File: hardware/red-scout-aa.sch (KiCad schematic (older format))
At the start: 2 parts, among them U1 SM200

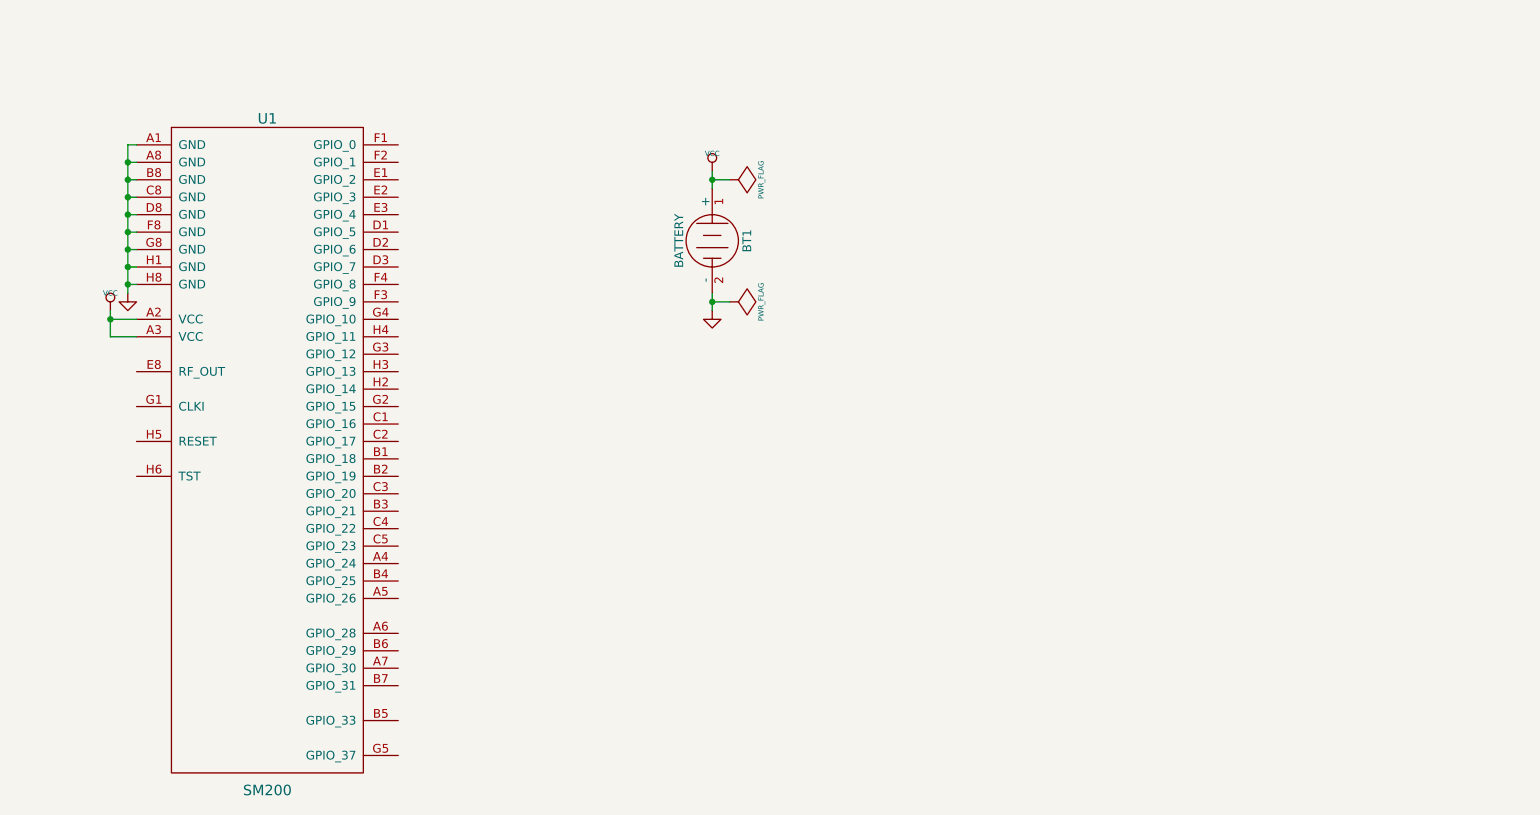
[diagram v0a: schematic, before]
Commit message: Added snap connectors and LEDs.
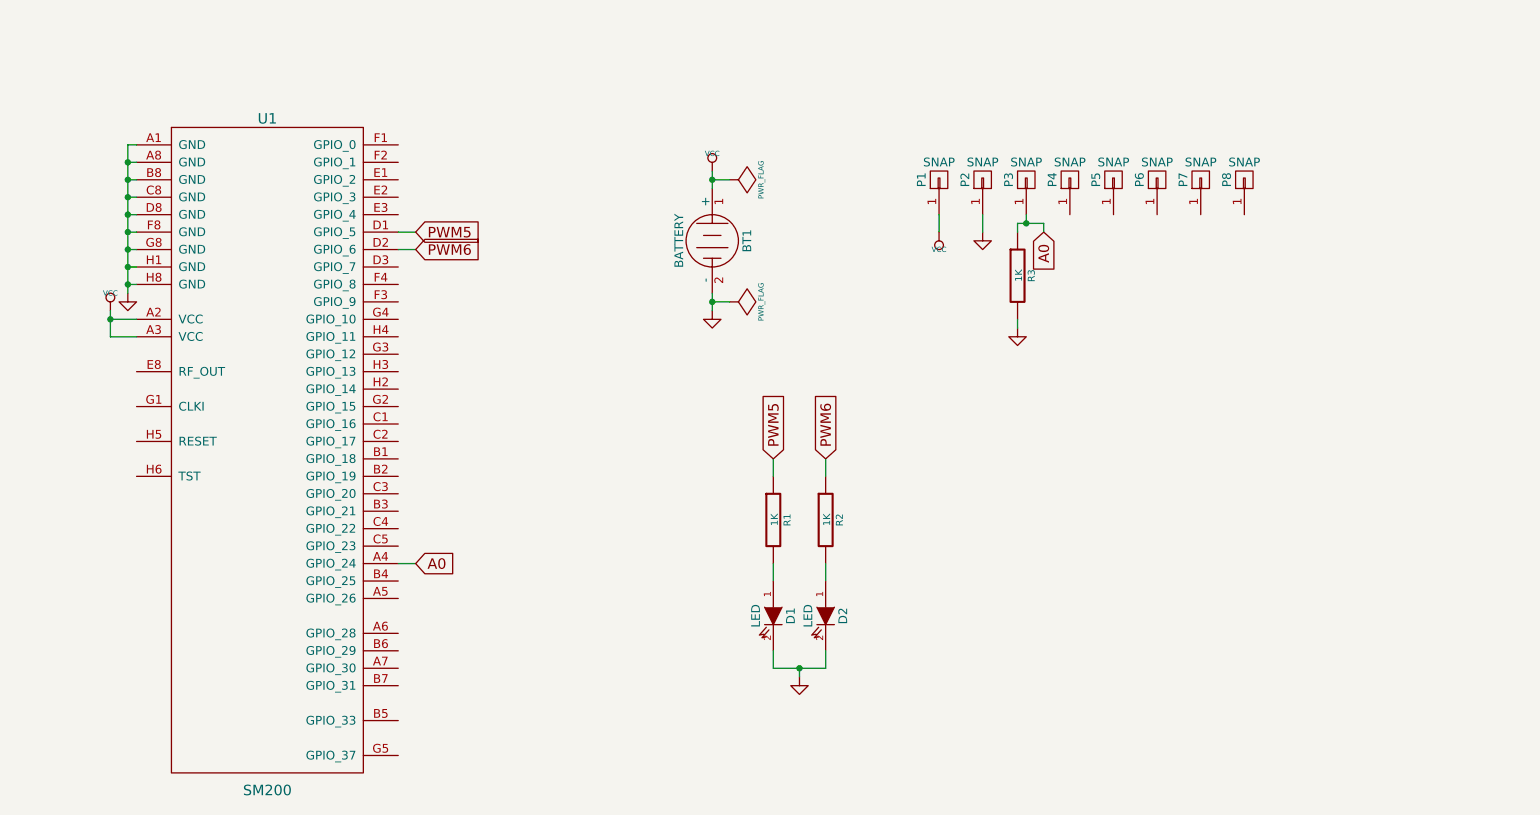
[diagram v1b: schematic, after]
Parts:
- added D1, D2: LED, symbol LED
- added P1, P2, P3, P4, P5, P6, P7, P8: SNAP, symbol CONN_01X01
- added R1, R2, R3: 1K, symbol R
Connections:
- net GND: now also D1.2 (K), D2.2 (K), P2.1 (P1), R3.2
- net VCC: now also P1.1 (P1)
- net A0: now reaches U1.A4 (GPIO_24)
- net A0: now also P3.1 (P1), R3.1
- net PWM5: now reaches U1.D1 (GPIO_5)
- net PWM5: now also R1.1
- net PWM6: now reaches U1.D2 (GPIO_6)
- net PWM6: now also R2.1
- new net: D1.1 (A), R1.2
- new net: D2.1 (A), R2.2
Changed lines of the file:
@@
 	1    0    0    -1
 $EndComp
-Wire Wire Line
-	2800 1550 2750 1550
-Wire Wire Line
-	2750 1550 2750 2400
-Wire Wire Line
-	2750 2350 2800 2350
-Wire Wire Line
-	2800 2250 2750 2250
-Connection ~ 2750 2250
-Wire Wire Line
-	2750 2150 2800 2150
-Connection ~ 2750 2150
-Wire Wire Line
-	2800 2050 2750 2050
-Connection ~ 2750 2050
-Wire Wire Line
-	2750 1950 2800 1950
-Connection ~ 2750 1950
-Wire Wire Line
-	2800 1850 2750 1850
-Connection ~ 2750 1850
-Wire Wire Line
-	2750 1750 2800 1750
-Connection ~ 2750 1750
-Wire Wire Line
-	2800 1650 2750 1650
-Connection ~ 2750 1650
-Connection ~ 2750 2350
 $Comp
 L BATTERY BT1
@@
 	1    0    0    -1
 $EndComp
-Wire Wire Line
-	6100 1800 6100 1700
-Wire Wire Line
-	6100 2400 6100 2500
 $Comp
 L VCC #PWR04
@@
 	1    0    0    -1
 $EndComp
-Wire Wire Line
-	2650 2500 2650 2650
-Wire Wire Line
-	2650 2550 2800 2550
-Wire Wire Line
-	2650 2650 2800 2650
-Connection ~ 2650 2550
 $Comp
 L PWR_FLAG #FLG05
@@
 	0    1    1    0
 $EndComp
+$Comp
+L R R3
+U 1 1 54F7F6ED
+P 7850 2300
+F 0 "R3" V 7930 2300 40  0000 C CNN
+F 1 "1K" V 7857 2301 40  0000 C CNN
+F 2 "" V 7780 2300 30  0000 C CNN
+F 3 "" H 7850 2300 30  0000 C CNN
+	1    7850 2300
+	1    0    0    -1
+$EndComp
+$Comp
+L CONN_01X01 P1
+U 1 1 54F7F75E
+P 7400 1750
+F 0 "P1" H 7400 1850 50  0000 C CNN
+F 1 "SNAP" V 7500 1750 50  0000 C CNN
+F 2 "" H 7400 1750 60  0000 C CNN
+F 3 "" H 7400 1750 60  0000 C CNN
+	1    7400 1750
+	0    -1   -1   0
+$EndComp
+$Comp
+L CONN_01X01 P2
+U 1 1 54F7F9DB
+P 7650 1750
+F 0 "P2" H 7650 1850 50  0000 C CNN
+F 1 "SNAP" V 7750 1750 50  0000 C CNN
+F 2 "" H 7650 1750 60  0000 C CNN
+F 3 "" H 7650 1750 60  0000 C CNN
+	1    7650 1750
+	0    -1   -1   0
+$EndComp
+$Comp
+L CONN_01X01 P3
+U 1 1 54F7FA0A
+P 7900 1750
+F 0 "P3" H 7900 1850 50  0000 C CNN
+F 1 "SNAP" V 8000 1750 50  0000 C CNN
+F 2 "" H 7900 1750 60  0000 C CNN
+F 3 "" H 7900 1750 60  0000 C CNN
+	1    7900 1750
+	0    -1   -1   0
+$EndComp
+$Comp
+L CONN_01X01 P4
+U 1 1 54F7FA10
+P 8150 1750
+F 0 "P4" H 8150 1850 50  0000 C CNN
+F 1 "SNAP" V 8250 1750 50  0000 C CNN
+F 2 "" H 8150 1750 60  0000 C CNN
+F 3 "" H 8150 1750 60  0000 C CNN
+	1    8150 1750
+	0    -1   -1   0
+$EndComp
+$Comp
+L CONN_01X01 P5
+U 1 1 54F7FAB5
+P 8400 1750
+F 0 "P5" H 8400 1850 50  0000 C CNN
+F 1 "SNAP" V 8500 1750 50  0000 C CNN
+F 2 "" H 8400 1750 60  0000 C CNN
+F 3 "" H 8400 1750 60  0000 C CNN
+	1    8400 1750
+	0    -1   -1   0
+$EndComp
+$Comp
+L CONN_01X01 P6
+U 1 1 54F7FABB
+P 8650 1750
+F 0 "P6" H 8650 1850 50  0000 C CNN
+F 1 "SNAP" V 8750 1750 50  0000 C CNN
+F 2 "" H 8650 1750 60  0000 C CNN
+F 3 "" H 8650 1750 60  0000 C CNN
+	1    8650 1750
+	0    -1   -1   0
+$EndComp
+$Comp
+L CONN_01X01 P7
+U 1 1 54F7FAC1
+P 8900 1750
+F 0 "P7" H 8900 1850 50  0000 C CNN
+F 1 "SNAP" V 9000 1750 50  0000 C CNN
+F 2 "" H 8900 1750 60  0000 C CNN
+F 3 "" H 8900 1750 60  0000 C CNN
+	1    8900 1750
+	0    -1   -1   0
+$EndComp
+$Comp
+L CONN_01X01 P8
+U 1 1 54F7FAC7
+P 9150 1750
+F 0 "P8" H 9150 1850 50  0000 C CNN
+F 1 "SNAP" V 9250 1750 50  0000 C CNN
+F 2 "" H 9150 1750 60  0000 C CNN
+F 3 "" H 9150 1750 60  0000 C CNN
+	1    9150 1750
+	0    -1   -1   0
+$EndComp
+$Comp
+L VCC #PWR07
+U 1 1 54F7FB25
+P 7400 2050
+F 0 "#PWR07" H 7400 2150 30  0001 C CNN
+F 1 "VCC" H 7400 2150 30  0000 C CNN
+F 2 "" H 7400 2050 60  0000 C CNN
+F 3 "" H 7400 2050 60  0000 C CNN
+	1    7400 2050
+	-1   0    0    1
+$EndComp
+$Comp
+L GND #PWR08
+U 1 1 54F7FB90
+P 7650 2050
+F 0 "#PWR08" H 7650 2050 30  0001 C CNN
+F 1 "GND" H 7650 1980 30  0001 C CNN
+F 2 "" H 7650 2050 60  0000 C CNN
+F 3 "" H 7650 2050 60  0000 C CNN
+	1    7650 2050
+	1    0    0    -1
+$EndComp
+Text GLabel 8000 2050 3    60   Input ~ 0
+A0
+$Comp
+L GND #PWR09
+U 1 1 54F7FDCC
+P 7850 2600
+F 0 "#PWR09" H 7850 2600 30  0001 C CNN
+F 1 "GND" H 7850 2530 30  0001 C CNN
+F 2 "" H 7850 2600 60  0000 C CNN
+F 3 "" H 7850 2600 60  0000 C CNN
+	1    7850 2600
+	1    0    0    -1
+$EndComp
+Wire Wire Line
+	2800 1550 2750 1550
+Wire Wire Line
+	2750 1550 2750 2400
+Wire Wire Line
+	2750 2350 2800 2350
+Wire Wire Line
+	2800 2250 2750 2250
+Connection ~ 2750 2250
+Wire Wire Line
+	2750 2150 2800 2150
+Connection ~ 2750 2150
+Wire Wire Line
+	2800 2050 2750 2050
+Connection ~ 2750 2050
+Wire Wire Line
+	2750 1950 2800 1950
+Connection ~ 2750 1950
+Wire Wire Line
+	2800 1850 2750 1850
+Connection ~ 2750 1850
+Wire Wire Line
+	2750 1750 2800 1750
+Connection ~ 2750 1750
+Wire Wire Line
+	2800 1650 2750 1650
+Connection ~ 2750 1650
+Connection ~ 2750 2350
+Wire Wire Line
+	6100 1700 6100 1800
+Wire Wire Line
+	6100 2400 6100 2500
+Wire Wire Line
+	2650 2500 2650 2650
+Wire Wire Line
+	2650 2550 2800 2550
+Wire Wire Line
+	2650 2650 2800 2650
+Connection ~ 2650 2550
 Wire Wire Line
 	6200 2450 6100 2450
@@
 	6200 1750 6100 1750
 Connection ~ 6100 1750
+Wire Wire Line
+	7900 1950 7900 2000
+Wire Wire Line
+	7850 2000 8000 2000
+Wire Wire Line
+	7850 2000 7850 2050
+Wire Wire Line
+	8000 2000 8000 2050
+Connection ~ 7900 2000
+Wire Wire Line
+	7850 2550 7850 2600
+Text GLabel 4400 3950 2    60   Input ~ 0
+A0
+Wire Wire Line
+	4300 3950 4400 3950
+Wire Wire Line
+	7400 1950 7400 2050
+Wire Wire Line
+	7650 2050 7650 1950
+$Comp
+L R R1
+U 1 1 54F80350
+P 6450 3700
+F 0 "R1" V 6530 3700 40  0000 C CNN
+F 1 "1K" V 6457 3701 40  0000 C CNN
+F 2 "" V 6380 3700 30  0000 C CNN
+F 3 "" H 6450 3700 30  0000 C CNN
+	1    6450 3700
+	1    0    0    -1
+$EndComp
+$Comp
+L R R2
+U 1 1 54F803F7
+P 6750 3700
+F 0 "R2" V 6830 3700 40  0000 C CNN
+F 1 "1K" V 6757 3701 40  0000 C CNN
+F 2 "" V 6680 3700 30  0000 C CNN
+F 3 "" H 6750 3700 30  0000 C CNN
+	1    6750 3700
+	1    0    0    -1
+$EndComp
+$Comp
+L LED D1
+U 1 1 54F80470
+P 6450 4250
+F 0 "D1" H 6450 4350 50  0000 C CNN
+F 1 "LED" H 6450 4150 50  0000 C CNN
+F 2 "" H 6450 4250 60  0000 C CNN
+F 3 "" H 6450 4250 60  0000 C CNN
+	1    6450 4250
+	0    1    1    0
+$EndComp
+$Comp
+L LED D2
+U 1 1 54F804AB
+P 6750 4250
+F 0 "D2" H 6750 4350 50  0000 C CNN
+F 1 "LED" H 6750 4150 50  0000 C CNN
+F 2 "" H 6750 4250 60  0000 C CNN
+F 3 "" H 6750 4250 60  0000 C CNN
+	1    6750 4250
+	0    1    1    0
+$EndComp
+Wire Wire Line
+	6450 3950 6450 4050
+Wire Wire Line
+	6750 4050 6750 3950
+Wire Wire Line
+	6450 4450 6450 4550
+Wire Wire Line
+	6450 4550 6750 4550
+Wire Wire Line
+	6750 4550 6750 4450
+$Comp
+L GND #PWR010
+U 1 1 54F805DF
+P 6600 4600
+F 0 "#PWR010" H 6600 4600 30  0001 C CNN
+F 1 "GND" H 6600 4530 30  0001 C CNN
+F 2 "" H 6600 4600 60  0000 C CNN
+F 3 "" H 6600 4600 60  0000 C CNN
+	1    6600 4600
+	1    0    0    -1
+$EndComp
+Wire Wire Line
+	6600 4600 6600 4550
+Connection ~ 6600 4550
+Text GLabel 6450 3350 1    60   Input ~ 0
+PWM5
+Text GLabel 6750 3350 1    60   Input ~ 0
+PWM6
+Text GLabel 4400 2050 2    60   Input ~ 0
+PWM5
+Text GLabel 4400 2150 2    60   Input ~ 0
+PWM6
+Wire Wire Line
+	4300 2050 4400 2050
+Wire Wire Line
+	4400 2150 4300 2150
+Wire Wire Line
+	6450 3350 6450 3450
+Wire Wire Line
+	6750 3350 6750 3450
 $EndSCHEMATC

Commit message: Wired up the snaps and nc'ed the unused pins.
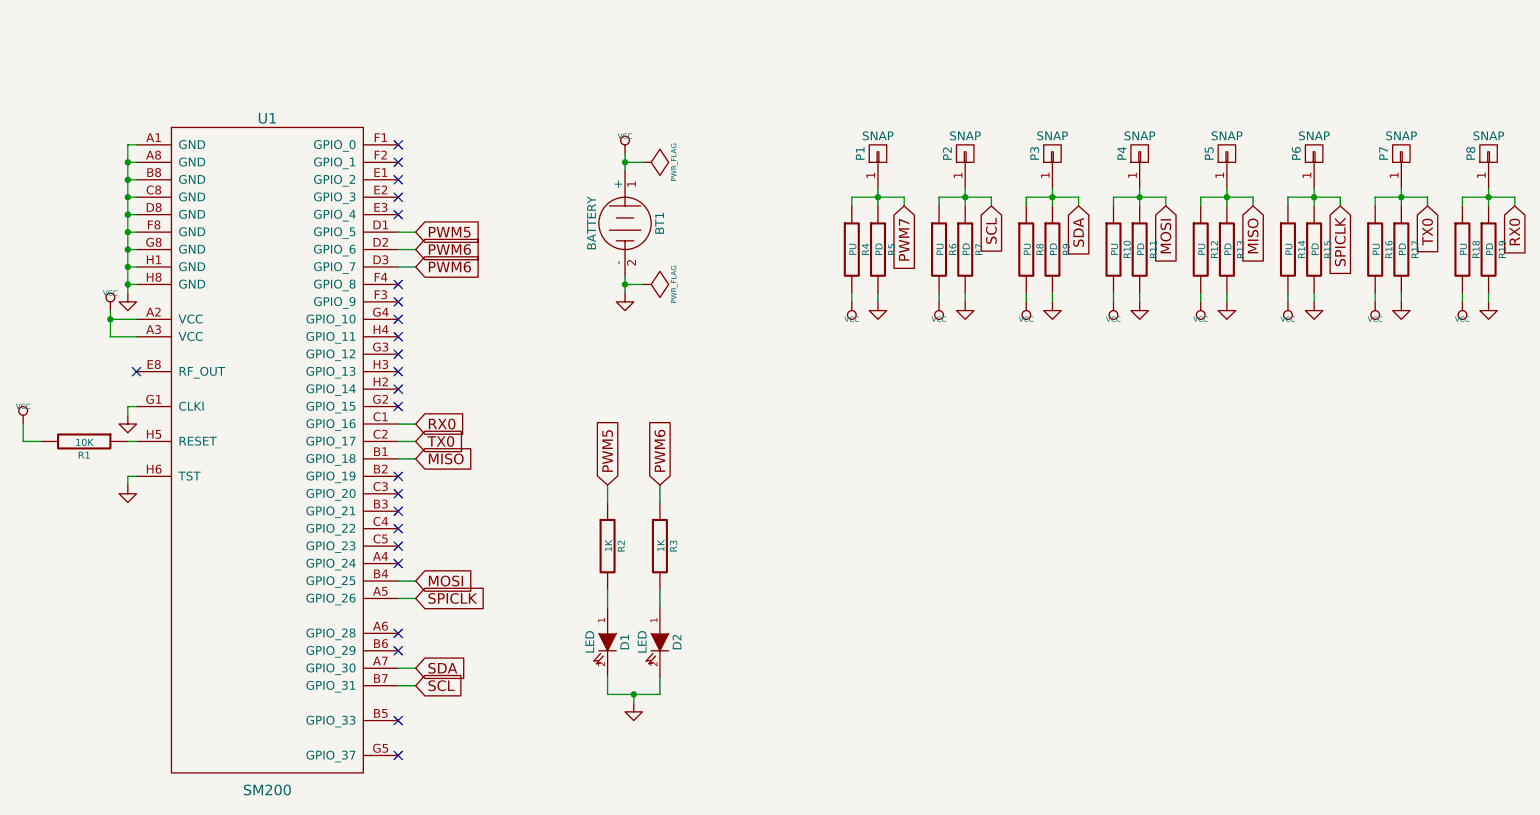
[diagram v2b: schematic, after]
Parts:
- removed P2: SNAP, symbol CONN_01X01
- added P3: SNAP, symbol CONN_01X01
- added R1: 10K, symbol R
- added R10, R12, R14, R16, R18, R4, R6, R8: PU, symbol R
- added R11, R13, R15, R17, R19, R5, R9: PD, symbol R
- R7: renamed from R3; value 1K -> PD
- renumbered P3 to P2, R1 to R2, R2 to R3
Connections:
- net GND: now also U1.G1 (CLKI), U1.H6 (TST), R11.2, R13.2, R15.2, R17.2, R19.2, R5.2, R9.2
- net PWM6: now also U1.D3 (GPIO_7)
- net VCC: now also R1.2, R10.2, R12.2, R14.2, R16.2, R18.2, R4.2, R6.2, R8.2; no longer P1.1 (P1)
- net SPICLK: now reaches U1.A5 (GPIO_26)
- net SPICLK: now also P6.1 (P1), R14.1, R15.1
- net SDA: now reaches U1.A7 (GPIO_30)
- net SDA: now also P3.1 (P1), R8.1, R9.1
- net MISO: now reaches U1.B1 (GPIO_18)
- net MISO: now also P5.1 (P1), R12.1, R13.1
- net MOSI: now reaches U1.B4 (GPIO_25)
- net MOSI: now also P4.1 (P1), R10.1, R11.1
- net SCL: now reaches U1.B7 (GPIO_31)
- net SCL: now also P2.1 (P1), R7.1, R6.1
- net RX0: now reaches U1.C1 (GPIO_16)
- net RX0: now also P8.1 (P1), R18.1, R19.1
- net TX0: now reaches U1.C2 (GPIO_17)
- net TX0: now also P7.1 (P1), R16.1, R17.1
- net at U1.H5 (RESET): now also R1.1
- removed net A0: P2.1 (P1), R7.1, U1.A4 (GPIO_24)
- new net PWM7: P1.1 (P1), R4.1, R5.1
- no-connect marks 0 -> 24
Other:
- moved on the sheet: BT1, D1, D2, P2, R2, R3, R7
